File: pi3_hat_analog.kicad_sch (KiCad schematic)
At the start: 26 parts, among them J3 Raspberry_Pi_2_3, J4 SJ1-3533NG, J5 SJ1-3533NG, J6 SJ1-3533NG, J7 SJ1-3533NG

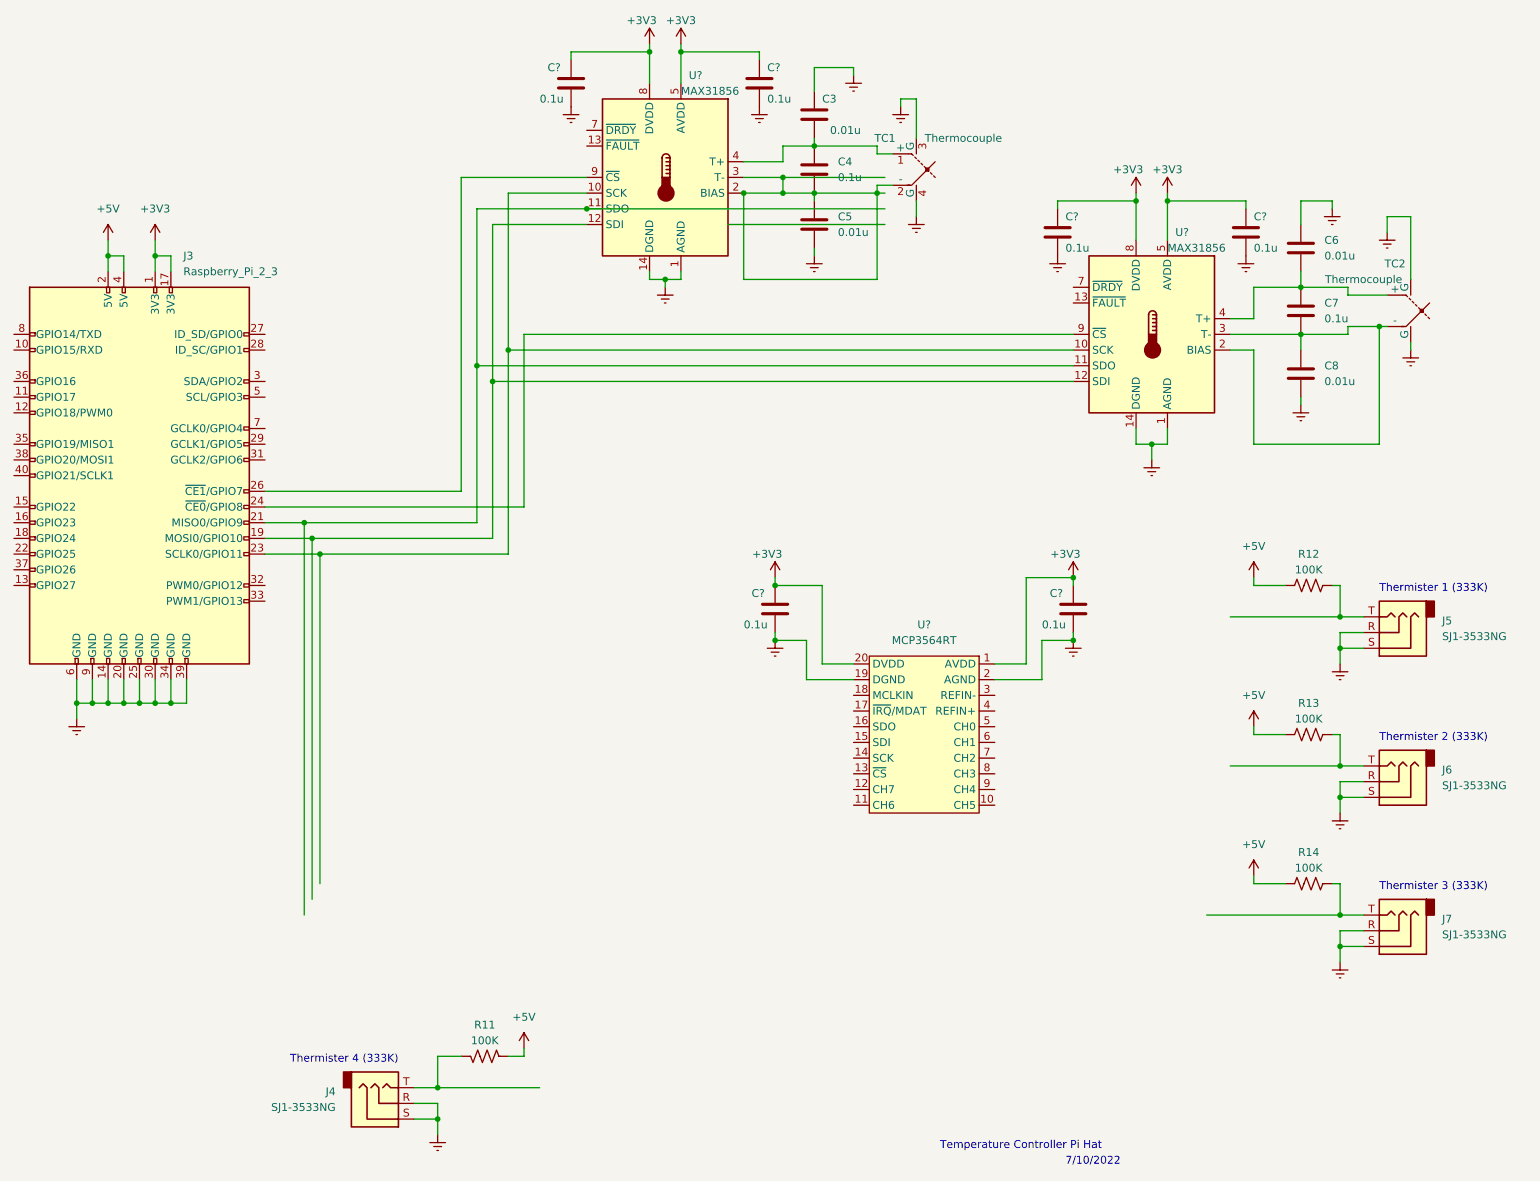
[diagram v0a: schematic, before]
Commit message: added thermister connections to A2D
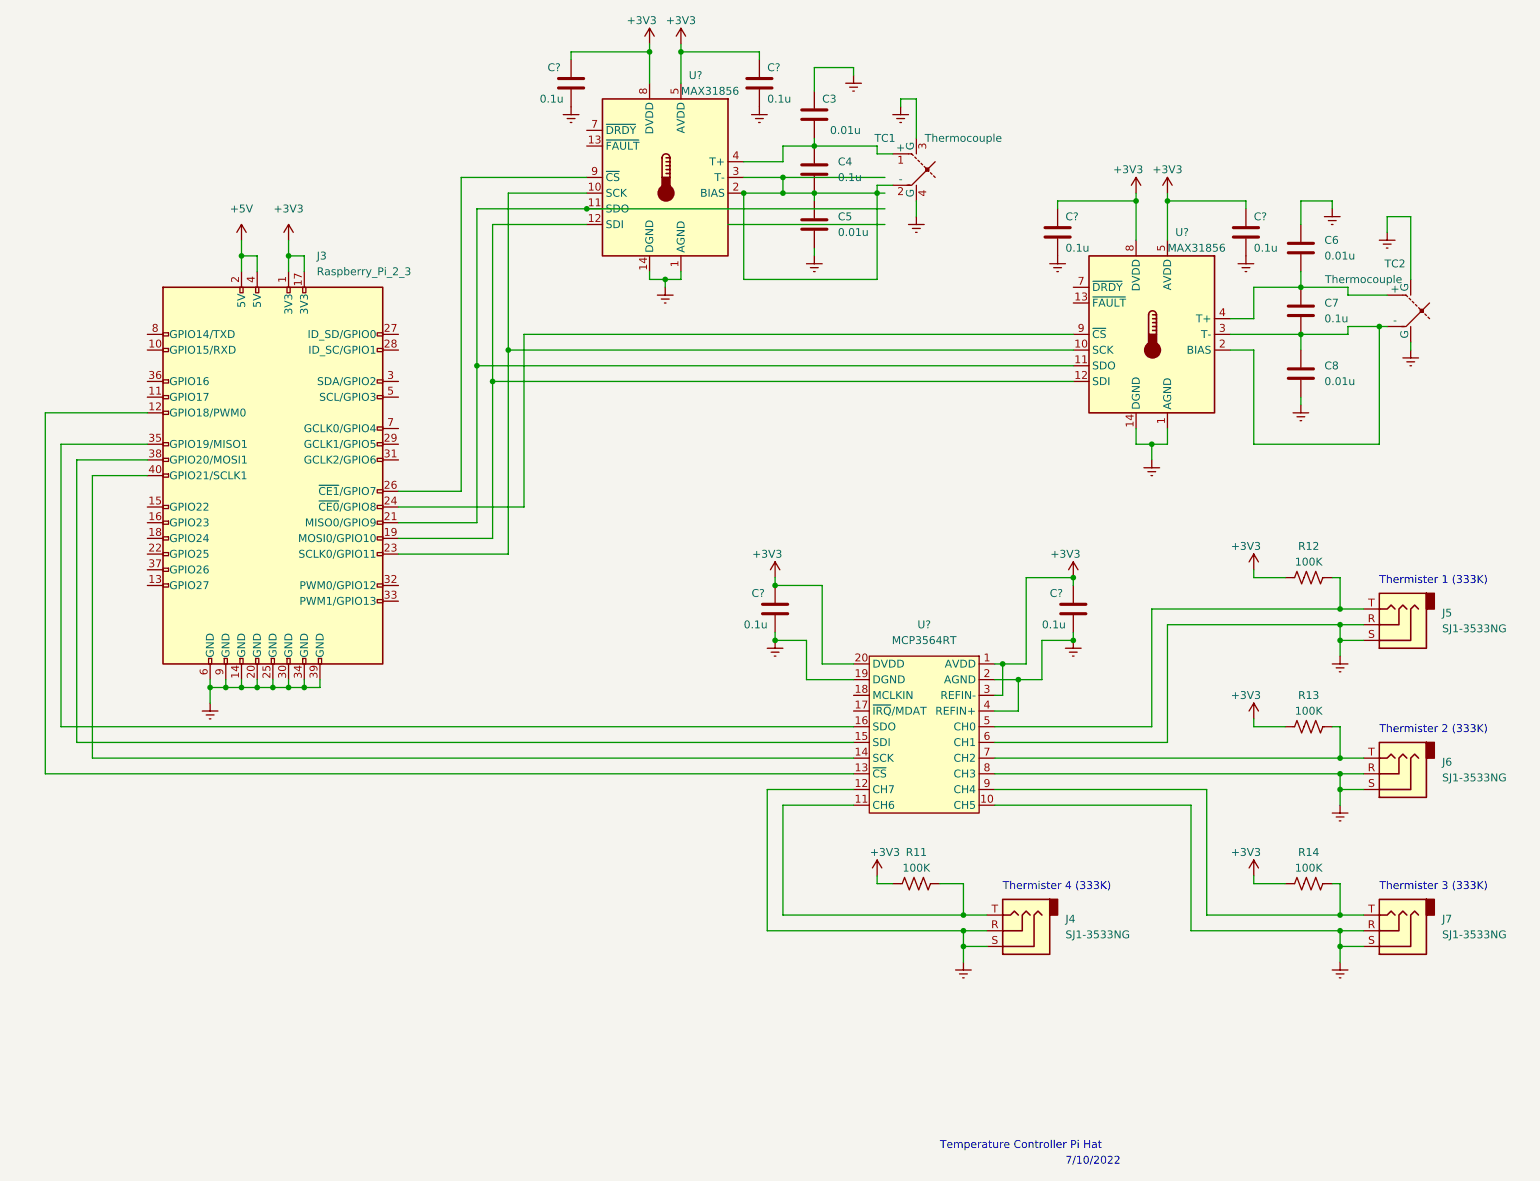
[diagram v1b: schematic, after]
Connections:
- net +3V3: now also R11.1, R12.1, R13.1, R14.1, U?.3 (REFIN-)
- net +5V: no longer R11.1, R12.1, R13.1, R14.1
- net GNDREF: now also U?.10 (CH5), U?.12 (CH7), U?.4 (REFIN+), U?.6 (CH1), U?.8 (CH3)
- net at J5.T, R12.2: now also U?.5 (CH0)
- net at J7.T, R14.2: now also U?.9 (CH4)
- net at J6.T, R13.2: now also U?.7 (CH2)
- net at J4.T, R11.2: now also U?.11 (CH6)
- net at J3.12 (GPIO18/PWM0): now also U?.13 (~{CS})
- net at J3.35 (GPIO19/MISO1): now also U?.16 (SDO)
- net at J3.38 (GPIO20/MOSI1): now also U?.15 (SDI)
- net at J3.40 (GPIO21/SCLK1): now also U?.14 (SCK)
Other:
- moved on the sheet: J3, J4, J5, J6, R11, R12, R13

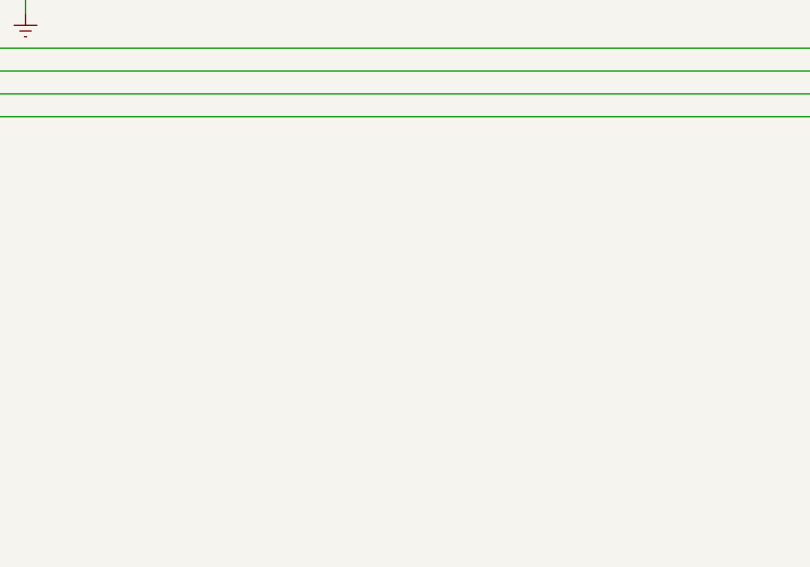
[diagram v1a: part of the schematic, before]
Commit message: added relay connector
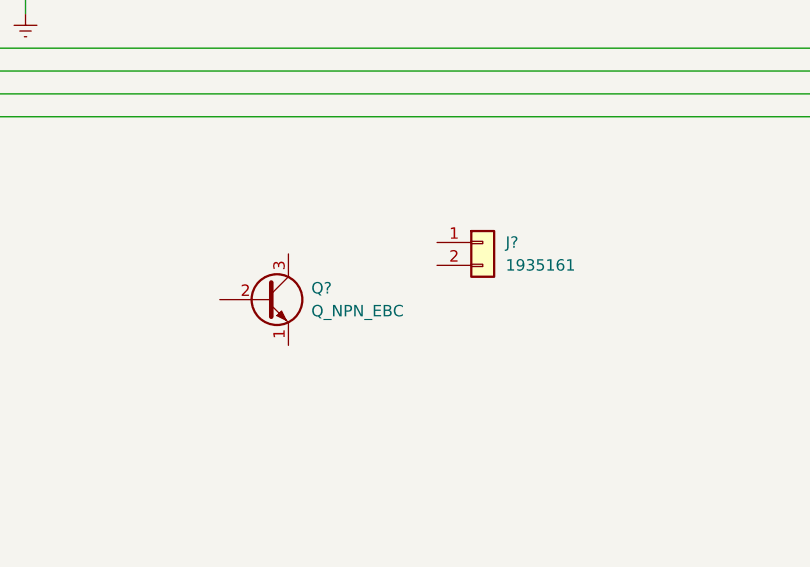
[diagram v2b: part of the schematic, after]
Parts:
- added J?: 1935161, symbol Connector_Generic:Conn_01x02
- added Q?: Q_NPN_EBC, symbol Device:Q_NPN_EBC
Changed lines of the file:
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@@
     (pin "9")
+  )
+  (symbol (lib_id "Connector_Generic:Conn_01x02") (at 102.87 149.86 0) (unit 1)
+    (in_bom yes) (on_board yes) (fields_autoplaced)
+    (property "Reference" "J?" (id 0) (at 105.41 149.8599 0)
+      (effects (font (size 1.27 1.27)) (justify left))
+    )
+    (property "Value" "1935161" (id 1) (at 105.41 152.3999 0)
+      (effects (font (size 1.27 1.27)) (justify left))
+    )
+    (property "Footprint" "" (id 2) (at 102.87 149.86 0)
+      (effects (font (size 1.27 1.27)) hide)
+    )
+    (property "Datasheet" "~" (id 3) (at 102.87 149.86 0)
+      (effects (font (size 1.27 1.27)) hide)
+    )
+    (pin "1")
+    (pin "2")
   )
   (symbol (lib_name "C_2") (lib_id "Device:C") (at 228.6 60.96 0) (unit 1)
@@
     (pin "1")
     (pin "2")
+  )
+  (symbol (lib_id "Device:Q_NPN_EBC") (at 78.74 156.21 0) (unit 1)
+    (in_bom yes) (on_board yes) (fields_autoplaced)
+    (property "Reference" "Q?" (id 0) (at 83.82 154.9399 0)
+      (effects (font (size 1.27 1.27)) (justify left))
+    )
+    (property "Value" "Q_NPN_EBC" (id 1) (at 83.82 157.4799 0)
+      (effects (font (size 1.27 1.27)) (justify left))
+    )
+    (property "Footprint" "" (id 2) (at 83.82 153.67 0)
+      (effects (font (size 1.27 1.27)) hide)
+    )
+    (property "Datasheet" "~" (id 3) (at 78.74 156.21 0)
+      (effects (font (size 1.27 1.27)) hide)
+    )
+    (pin "1")
+    (pin "2")
+    (pin "3")
   )
   (symbol (lib_id "Connector:AudioJack3") (at 243.84 161.29 180) (unit 1)
@@
       (reference "J7") (unit 1) (value "SJ1-3533NG") (footprint "Connector_Audio:Jack_3.5mm_CUI_SJ1-3533NG_Horizontal")
     )
+    (path "/aa9c9fa8-922d-4661-b6ba-f949438fcd13"
+      (reference "J?") (unit 1) (value "1935161") (footprint "")
+    )
+    (path "/f17ac7f1-ed89-442c-9bef-8a53af152a56"
+      (reference "Q?") (unit 1) (value "Q_NPN_EBC") (footprint "")
+    )
     (path "/b54a2c4a-5916-4341-82f2-1d8f0206007c"

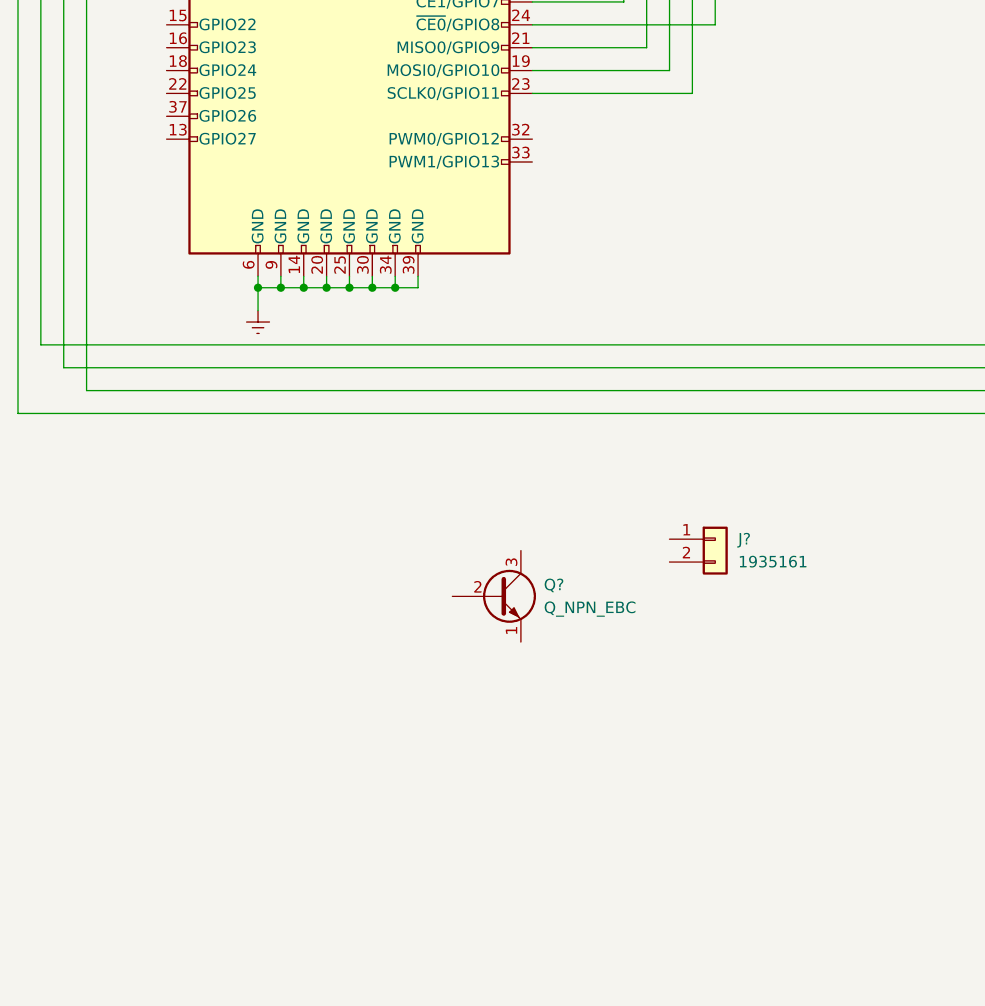
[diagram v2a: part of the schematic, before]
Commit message: added footprints for relay circuit
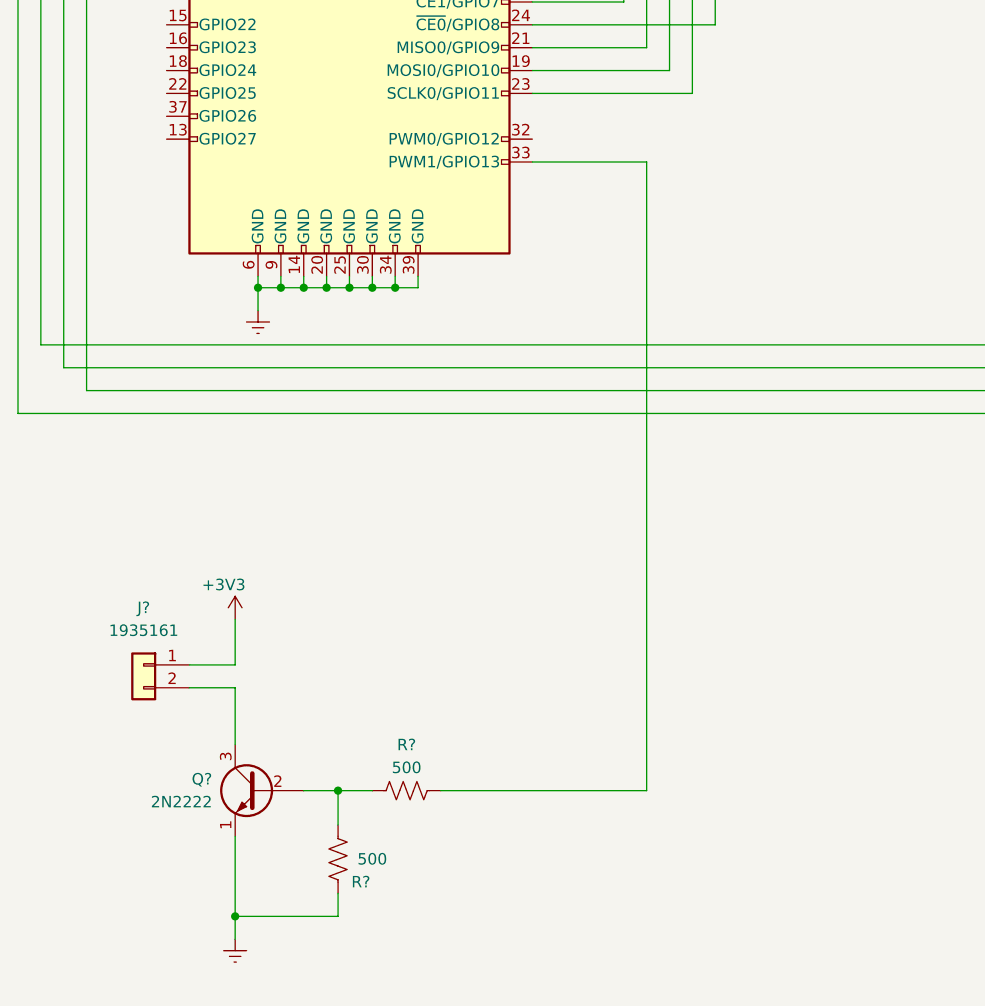
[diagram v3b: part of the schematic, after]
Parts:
- added R? (x2): 500, Resistor_SMD:R_0201_0603Metric_Pad0.64x0.40mm_HandSolder, symbol Device:R_US
- Q?: value Q_NPN_EBC -> 2N2222
- R11, R12, R13, R14: footprint Resistor_THT:R_Axial_DIN0411_L9.9mm_D3.6mm_P12.70mm_Horizontal -> Resistor_SMD:R_0201_0603Metric_Pad0.64x0.40mm_HandSolder
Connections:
- net +3V3: now also J?.1 (Pin_1)
- net GNDREF: now also Q?.1 (E), R?.2
- net at J3.33 (PWM1/GPIO13): now also R?.2
- net at J?.2 (Pin_2): now also Q?.3 (C)
- net at Q?.2 (B): now also R?.1, R?.1
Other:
- moved on the sheet: J?, Q?

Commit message: added thermocouple footprint.  Initial board layout.
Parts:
- J1: renamed from J?; footprint (none) -> Connector_Phoenix_MSTB:PhoenixContact_MSTBVA_2,5_2-G_1x02_P5.00mm_Vertical
- Q1: renamed from Q?; value 2N2222 -> 2N3904BU; footprint (none) -> Package_TO_SOT_THT:TO-92_Inline
- U2: renamed from U?; footprint (none) -> Package_SO:TSSOP-20_4.4x6.5mm_P0.65mm
- gave numbers to parts that had none: 10
